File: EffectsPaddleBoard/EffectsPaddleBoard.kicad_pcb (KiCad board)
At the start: 4 copper layers, 89.6 x 66.6 mm, 90 parts, among them J1 Conn_01x03_Pin, J2 Conn_01x06_Pin, J3 Barrel_Jack, J4 Conn_01x04_Pin, J5 AudioJack2, J6 AudioJack2, SW1 SW_SPDT, SW2 SW_Push, SW4 SW_Push, U1 STM32F405RGTx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

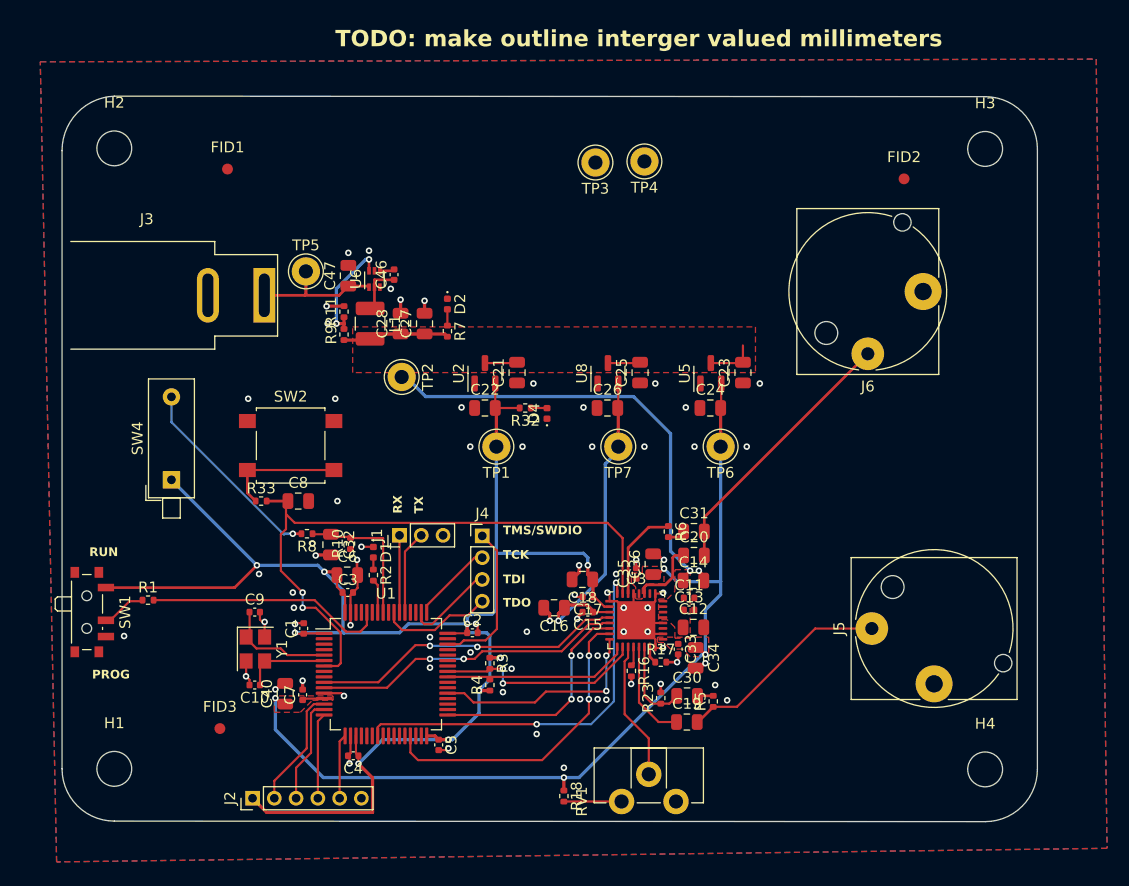
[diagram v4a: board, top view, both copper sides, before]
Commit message: Begun with double sided layout
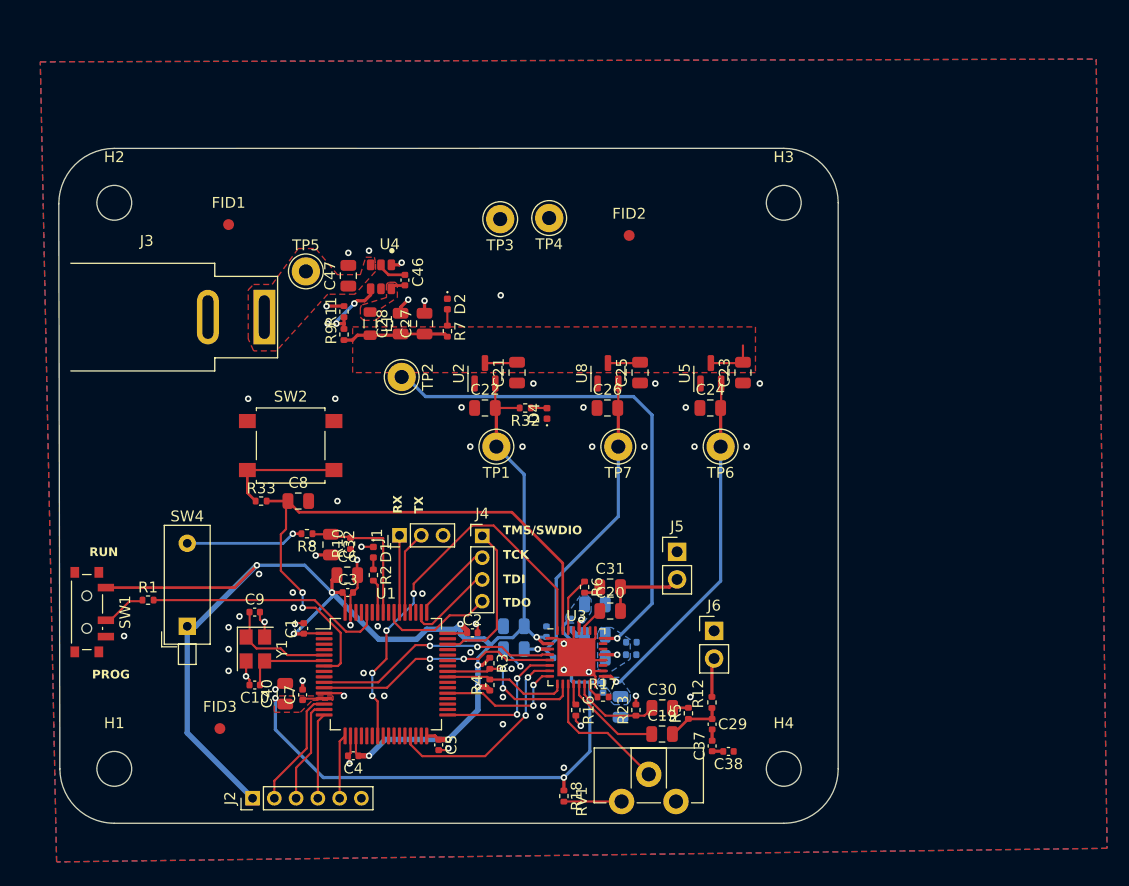
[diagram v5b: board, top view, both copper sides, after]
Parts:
- removed U6: AP62250Z6, Package_TO_SOT_SMD:SOT-563
- added C29: 100n, Capacitor_SMD:C_0402_1005Metric, F.Cu at (182.4, 104.9)
- added C37: 100n, Capacitor_SMD:C_0402_1005Metric, F.Cu at (182.4, 106.9)
- added C38: 100n, Capacitor_SMD:C_0402_1005Metric, F.Cu at (183.9, 107.4)
- added R12: 220, Resistor_SMD:R_0402_1005Metric, F.Cu at (182.4, 102.9)
- added U4: AP62200WU-7, EffectsPaddleBoard:TSOT26, F.Cu at (152.0, 63.8)
- C11, C12, C13, C14, C15, C16, C17, C18, C33, C34, C35, C36: moved to B.Cu
- J5, J6: value AudioJack2 -> Conn_01x02_Pin; footprint Connector_Audio:Jack_6.35mm_Neutrik_NJ2FD-V_Vertical -> Connector_PinHeader_2.54mm:PinHeader_1x02_P2.54mm_Vertical
- L1: value 2.2u -> 4.7u; footprint Inductor_SMD:L_1210_3225Metric -> Inductor_SMD:L_0805_2012Metric
- moved J6 29.1 mm to (182.6, 96.3), turned to 0 degrees
- moved FID2 25.8 mm to (174.8, 60.0)
- moved J5 19.2 mm to (179.2, 89.1), turned to 0 degrees
- moved H3 19.2 mm to (189.0, 57.0)
- moved H4 18.5 mm to (189.0, 109.0)
- moved SW4 13.5 mm to (134.2, 95.9)
- moved C14 10.3 mm to (171.7, 96.7), turned to 180 degrees
- moved TP3 10.2 mm to (162.9, 58.5)
- moved TP4 10.2 mm to (167.4, 58.4)
- moved C12 9.47 mm to (171.7, 98.8), turned to 180 degrees
- moved R6 9.24 mm to (170.7, 92.3)
- moved C20 9.24 mm to (173.1, 94.5)
- moved C31 9.24 mm to (173.1, 92.3)
- moved C34 8.24 mm to (174.0, 103.3)
- moved C33 7.75 mm to (172.4, 101.5)
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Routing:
- net /Codec/AudioOutBoard: track 24.8 -> 7.69 mm
- net Net-(C19-Pad2): track 19.6 -> 5.15 mm
- net /Barreljack_in: track 12.3 -> 0.00 mm
- net +3.3V: track 153.5 -> 142.5 mm
- net I2S_CK: track 28.8 -> 19.2 mm
- net I2S_MCK: track 20.2 -> 12.1 mm
- net Net-(R8-Pad2): track 18.9 -> 10.9 mm
- net I2S_WS: track 20.8 -> 13.2 mm
- net I2S_SD: track 28.7 -> 22.4 mm
- net I2S_ext_SD: track 28.8 -> 22.6 mm
- net GND: track 54.8 -> 49.1 mm, vias 74 -> 65
- net I2C_SDA: track 17.1 -> 11.4 mm
- net I2C_SCL: track 19.3 -> 14.1 mm
- net /Codec/HPL: track 6.46 -> 2.38 mm
- net Net-(J6-Pin_2): track 0.00 -> 3.61 mm
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- added copper zone on B.Cu, net +3.3VA
- added copper zone on B.Cu, net +5V
- added copper zone on F.Cu, net /Barreljack_in
- added copper zone on F.Cu, net /v_sw
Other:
- board size 89.6 x 66.6 mm -> 71.6 x 62 mm
- board text removed: "TODO: make outline interger valued millimeters"

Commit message: Upgraded to kicad8 and improved layout
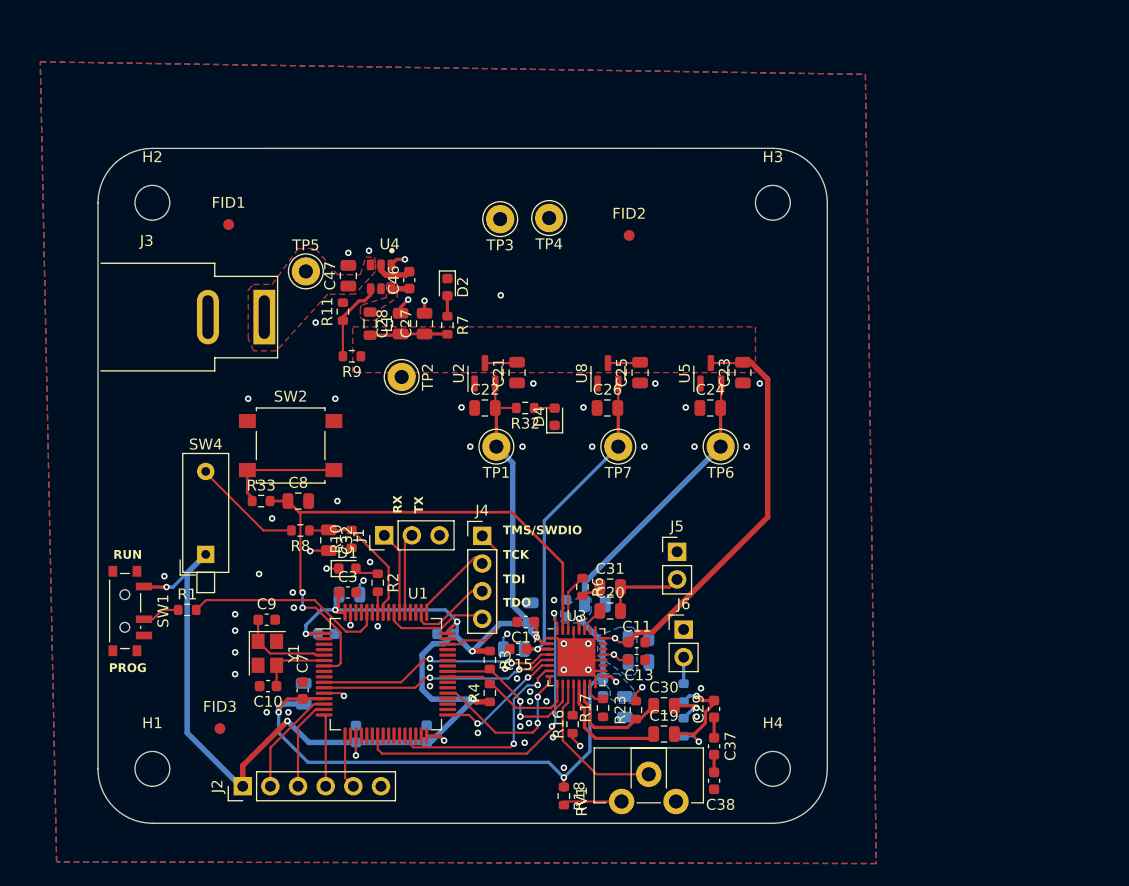
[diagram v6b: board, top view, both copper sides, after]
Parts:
- C1, C2, C4, C5: footprint Capacitor_SMD:C_0402_1005Metric -> Capacitor_SMD:C_0603_1608Metric; moved to B.Cu
- C10, C29, C3, C33, C35, C37, C38, C46, C7, C9: footprint Capacitor_SMD:C_0402_1005Metric -> Capacitor_SMD:C_0603_1608Metric
- C11, C13, C15, C17: footprint Capacitor_SMD:C_0402_1005Metric -> Capacitor_SMD:C_0603_1608Metric; moved to F.Cu
- C40, C6: moved to B.Cu
- D1, D2, D4: footprint LED_SMD:LED_0402_1005Metric -> LED_SMD:LED_0603_1608Metric
- J1: footprint Connector_PinHeader_2.00mm:PinHeader_1x03_P2.00mm_Vertical -> Connector_PinHeader_2.54mm:PinHeader_1x03_P2.54mm_Vertical
- J2: footprint Connector_PinHeader_2.00mm:PinHeader_1x06_P2.00mm_Vertical -> Connector_PinHeader_2.54mm:PinHeader_1x06_P2.54mm_Vertical
- J4: footprint Connector_PinHeader_2.00mm:PinHeader_1x04_P2.00mm_Vertical -> Connector_PinHeader_2.54mm:PinHeader_1x04_P2.54mm_Vertical
- R1, R10, R11, R16, R17, R18, R2, R23, R3, R32, R33, R4, R6, R7, R8, R9: footprint Resistor_SMD:R_0402_1005Metric -> Resistor_SMD:R_0603_1608Metric
- R12, R5: footprint Resistor_SMD:R_0402_1005Metric -> Resistor_SMD:R_0603_1608Metric; moved to B.Cu
- moved SW4 6.82 mm to (135.9, 89.3)
- moved C12 4.02 mm to (175.7, 99.2), turned to 0 degrees
- moved C14 4.01 mm to (175.7, 97.0), turned to 0 degrees
- moved C15 3.79 mm to (164.6, 98.0), turned to 180 degrees
- moved R1 3.71 mm to (134.2, 94.4)
- moved SW1 3.50 mm to (128.8, 94.5)
- moved H1 3.50 mm to (131.0, 109.0)
- moved H2 3.50 mm to (131.0, 57.0)
- moved C38 3.01 mm to (182.6, 110.1), turned to 90 degrees
- moved D1 2.82 mm to (148.9, 90.6), turned to 0 degrees
- moved J6 2.80 mm to (179.8, 96.2)
- moved R12 2.75 mm to (179.8, 102.0)
- moved C2 2.48 mm to (157.9, 96.6), turned to 180 degrees
- moved C1 2.13 mm to (147.0, 96.6), turned to 0 degrees
- moved R9 2.13 mm to (149.3, 71.1), turned to 180 degrees
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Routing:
- net GND: track 49.1 -> 31.7 mm, vias 65 -> 63
- net +5V: track 68.4 -> 53.7 mm
- net Codec_GPIO: track 37.4 -> 30.8 mm, vias 4 -> 2
- net Net-(C19-Pad2): track 5.15 -> 11.3 mm, vias 0 -> 2
- net +3.3VA: track 88.9 -> 84.9 mm
- net Net-(U1-BOOT0): track 22.2 -> 18.7 mm
- net I2S_MCK: track 12.1 -> 15.1 mm
- net /Codec/Analog_In_R: track 8.26 -> 10.7 mm
- net Net-(C30-Pad2): track 1.44 -> 3.73 mm, vias 0 -> 1
- net /Codec/Analog_In_L: track 9.18 -> 11.1 mm
- net Codec_Reset: track 55.3 -> 53.6 mm
- net /Codec/Volume: track 12.9 -> 14.6 mm
- net I2C_SDA: track 11.4 -> 13.1 mm
- net I2C_SCL: track 14.1 -> 15.6 mm
- net I2S_WS: track 13.2 -> 11.9 mm
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- removed copper zone on F.Cu, net +3.3VA
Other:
- board size 71.6 x 62 mm -> 67 x 62 mm
